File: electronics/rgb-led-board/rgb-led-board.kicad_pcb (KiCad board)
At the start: 2 copper layers, 24.1 x 17.8 mm, 12 parts, among them P1 PAD_SOLDER_2mm, P2 PAD_SOLDER_2mm, P3 CONN_01X08, P4 PAD_SOLDER_2mm, P5 PAD_SOLDER_2mm, P6 PAD_SOLDER_2mm, P7 PAD_SOLDER_2mm, U1 AL1793AFE-13

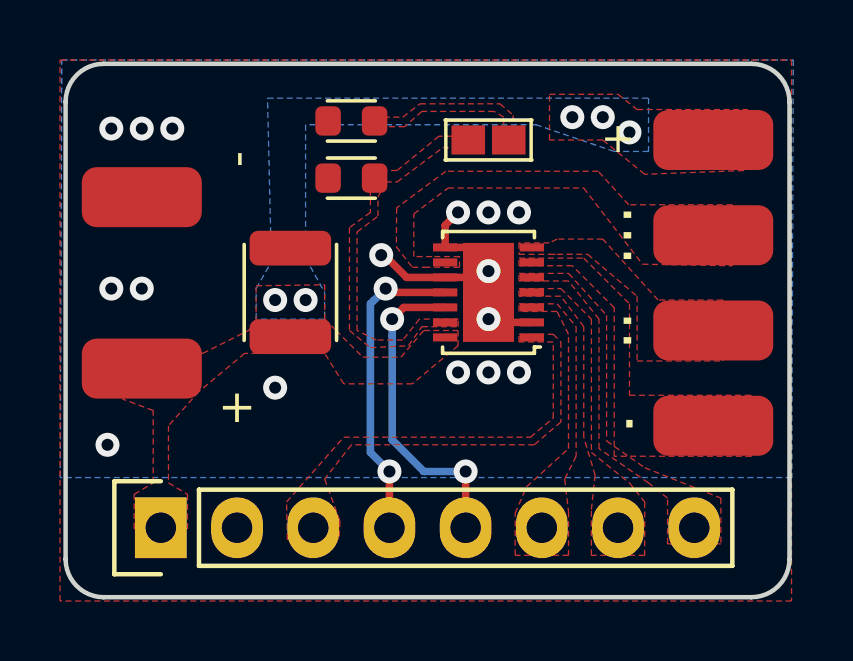
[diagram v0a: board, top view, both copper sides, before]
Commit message: Final changes to led driver board before gerbers
Minor annotation and titleblock contents
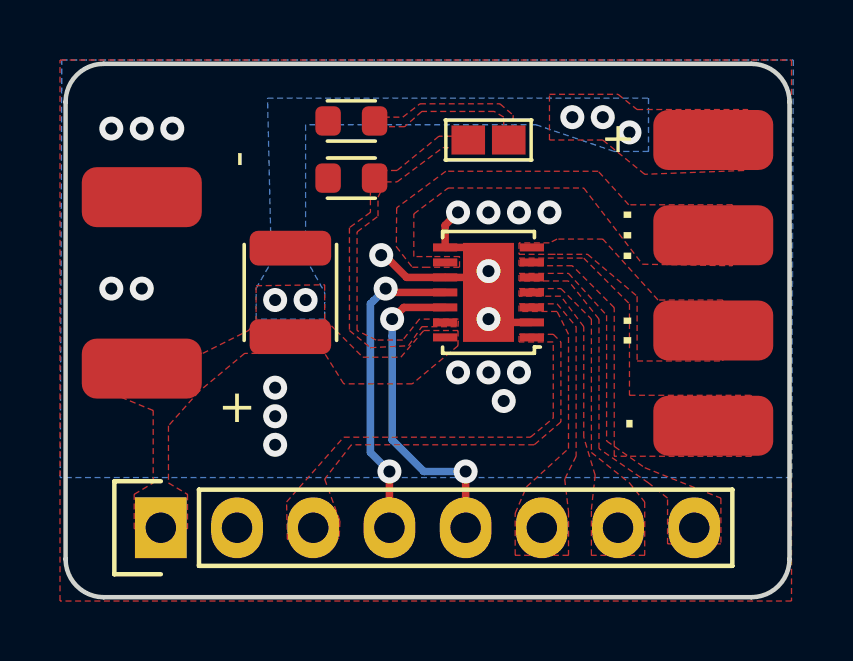
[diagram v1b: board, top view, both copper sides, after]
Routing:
- net GND: vias 16 -> 19
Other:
- board text added: "3x0.5A LED COMM ANODE SRAPSON 2018"
- board text added: "7-30V INPUT"
- board text added: "PCB Stackup 2 Layer 1.6mm FR4 ENIG Finish 25*18mm >0.35mm via drill >0.25mm clearance"
- board text removed: "2018 S.Rapson"
- board text removed: "max 30V"
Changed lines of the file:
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@@
   (general
     (thickness 1.6)
-    (drawings 24)
-    (tracks 52)
+    (drawings 27)
+    (tracks 55)
     (zones 0)
     (modules 12)
@@
   )
   (page A4)
+  (title_block
+    (title "3 channel common anode LED driver")
+    (date 2018-11-10)
+    (rev 1.0)
+    (company "Electric UI")
+    (comment 1 "Scott Rapson")
+  )
   (layers
     (0 F.Cu signal)
@@
     (visible_elements FFFDFF7F)
     (pcbplotparams
-      (layerselection 0x010fc_ffffffff)
-      (usegerberextensions false)
+      (layerselection 0x313fc_ffffffff)
+      (usegerberextensions true)
       (usegerberattributes false)
       (usegerberadvancedattributes false)
@@
       (outputformat 1)
       (mirror false)
-      (drillshape 1)
+      (drillshape 0)
       (scaleselection 1)
-      (outputdirectory ""))
+      (outputdirectory "Outputs/manf_exports/"))
   )
   (net 0 "")
@@
       (net 12 "Net-(R2-Pad1)"))
   )
-  (gr_text "2018\nS.Rapson" (at 144.145 58.547 90) (layer B.SilkS)
+  (gr_text "PCB Stackup\n\n2 Layer\n1.6mm FR4\nENIG Finish\n25*18mm\n>0.35mm via drill\n>0.25mm clearance" (at 157.0355 65.278) (layer Cmts.User)
+    (effects (font (size 1.5 1.5) (thickness 0.3)) (justify left))
+  )
+  (dimension 17.780113 (width 0.3) (layer Dwgs.User)
+    (gr_text "17.780 mm" (at 116.580656 66.69645 270.2046269) (layer Dwgs.User)
+      (effects (font (size 1.5 1.5) (thickness 0.3)))
+    )
+    (feature1 (pts (xy 122.6185 75.565) (xy 118.125976 75.581045)))
+    (feature2 (pts (xy 122.555 57.785) (xy 118.062476 57.801045)))
+    (crossbar (pts (xy 118.648893 57.79895) (xy 118.712393 75.57895)))
+    (arrow1a (pts (xy 118.712393 75.57895) (xy 118.121953 74.454548)))
+    (arrow1b (pts (xy 118.712393 75.57895) (xy 119.294787 74.450359)))
+    (arrow2a (pts (xy 118.648893 57.79895) (xy 118.066499 58.927541)))
+    (arrow2b (pts (xy 118.648893 57.79895) (xy 119.239333 58.923352)))
+  )
+  (dimension 24.1935 (width 0.3) (layer Dwgs.User)
+    (gr_text "24.194 mm" (at 134.65175 51.5575) (layer Dwgs.User)
+      (effects (font (size 1.5 1.5) (thickness 0.3)))
+    )
+    (feature1 (pts (xy 146.7485 57.7215) (xy 146.7485 53.071079)))
+    (feature2 (pts (xy 122.555 57.7215) (xy 122.555 53.071079)))
+    (crossbar (pts (xy 122.555 53.6575) (xy 146.7485 53.6575)))
+    (arrow1a (pts (xy 146.7485 53.6575) (xy 145.621996 54.243921)))
+    (arrow1b (pts (xy 146.7485 53.6575) (xy 145.621996 53.071079)))
+    (arrow2a (pts (xy 122.555 53.6575) (xy 123.681504 54.243921)))
+    (arrow2b (pts (xy 122.555 53.6575) (xy 123.681504 53.071079)))
+  )
+  (gr_text "3x0.5A LED\nCOMM ANODE\nSRAPSON 2018" (at 143.7005 58.3565 90) (layer B.SilkS)
     (effects (font (size 1 1) (thickness 0.18)) (justify left mirror))
   )
-  (gr_text "max\n30V" (at 127 63.5 90) (layer B.SilkS)
+  (gr_text "7-30V\nINPUT" (at 127 62.6745 90) (layer B.SilkS)
     (effects (font (size 1.2 1.2) (thickness 0.2)) (justify mirror))
   )
@@
   (segment (start 135.207 64.905) (end 136.152 64.905) (width 0.25) (layer F.Cu) (net 1))
   (via (at 137.668 68.072) (size 0.8) (drill 0.4) (layers F.Cu B.Cu) (net 1))
-  (via (at 123.952 70.485) (size 0.8) (drill 0.4) (layers F.Cu B.Cu) (net 1))
   (via (at 125.095 59.944) (size 0.8) (drill 0.4) (layers F.Cu B.Cu) (net 1))
   (via (at 124.079 59.944) (size 0.8) (drill 0.4) (layers F.Cu B.Cu) (net 1))
@@
   (via (at 133.075742 64.16189) (size 0.8) (drill 0.4) (layers F.Cu B.Cu) (net 1))
   (segment (start 133.24989 64.16189) (end 133.075742 64.16189) (width 0.25) (layer F.Cu) (net 1))
-  (via (at 139.446 59.563) (size 0.8) (drill 0.4) (layers F.Cu B.Cu) (net 2))
-  (via (at 140.462 59.563) (size 0.8) (drill 0.4) (layers F.Cu B.Cu) (net 2))
-  (via (at 141.351 60.071) (size 0.8) (drill 0.4) (layers F.Cu B.Cu) (net 2))
   (segment (start 133.179886 64.16189) (end 133.075742 64.16189) (width 0.25) (layer F.Cu) (net 1))
   (segment (start 133.922996 64.905) (end 133.179886 64.16189) (width 0.25) (layer F.Cu) (net 1))
@@
   (segment (start 135.207 63.905) (end 135.207 63.167) (width 0.25) (layer F.Cu) (net 1))
   (segment (start 135.207 63.167) (end 135.636 62.738) (width 0.25) (layer F.Cu) (net 1))
+  (via (at 129.54 69.5325) (size 0.8) (drill 0.4) (layers F.Cu B.Cu) (net 1))
+  (via (at 129.54 70.485) (size 0.8) (drill 0.4) (layers F.Cu B.Cu) (net 1))
+  (via (at 137.16 69.0245) (size 0.8) (drill 0.4) (layers F.Cu B.Cu) (net 1))
+  (via (at 138.684 62.738) (size 0.8) (drill 0.4) (layers F.Cu B.Cu) (net 1))
+  (via (at 139.446 59.563) (size 0.8) (drill 0.4) (layers F.Cu B.Cu) (net 2))
+  (via (at 140.462 59.563) (size 0.8) (drill 0.4) (layers F.Cu B.Cu) (net 2))
+  (via (at 141.351 60.071) (size 0.8) (drill 0.4) (layers F.Cu B.Cu) (net 2))
   (via (at 130.556 65.659) (size 0.8) (drill 0.4) (layers F.Cu B.Cu) (net 2))
   (via (at 129.54 65.659) (size 0.8) (drill 0.4) (layers F.Cu B.Cu) (net 2))
@@
     (polygon
       (pts
-        (xy 124.841 73.279) (xy 124.841 72.136) (xy 125.476 71.755) (xy 125.476 69.342) (xy 124.46 68.961)
-        (xy 124.46 67.437) (xy 127.127 67.437) (xy 128.651 66.675) (xy 128.905 66.38925) (xy 128.905 65.18275)
+        (xy 124.841 73.279) (xy 124.841 72.136) (xy 125.476 71.755) (xy 125.476 69.342) (xy 123.6345 68.58)
+        (xy 123.698 67.3735) (xy 127.127 67.437) (xy 128.651 66.675) (xy 128.905 66.38925) (xy 128.905 65.18275)
         (xy 131.191 65.151) (xy 131.191 66.294) (xy 131.572 66.675) (xy 132.461 67.564) (xy 133.731 67.564)
         (xy 134.493 66.675) (xy 135.636 66.675) (xy 135.636 67.183) (xy 134.112 68.453) (xy 131.826 68.453)
@@
     (polygon
       (pts
-        (xy 125.222 75.692) (xy 125.222 73.152) (xy 146.812 73.152) (xy 146.812 75.692)
+        (xy 124.46 75.692) (xy 124.46 73.152) (xy 146.812 73.152) (xy 146.812 75.692)
       )
     )
@@
     (min_thickness 0.25)
     (keepout (tracks allowed) (vias allowed) (copperpour not_allowed))
-    (fill (arc_segments 32) (thermal_gap 0.25) (thermal_bridge_width 0.3) (smoothing fillet) (radius 2))
+    (fill (arc_segments 32) (thermal_gap 0.25) (thermal_bridge_width 0.3))
     (polygon
       (pts
@@
     (min_thickness 0.3)
     (keepout (tracks allowed) (vias allowed) (copperpour not_allowed))
-    (fill (arc_segments 32) (thermal_gap 0.508) (thermal_bridge_width 0.508) (smoothing fillet) (radius 1.5))
-    (polygon
-      (pts
-        (xy 130.429 60.071) (xy 131.826 60.071) (xy 131.826 61.214) (xy 130.429 61.214)
+    (fill (arc_segments 32) (thermal_gap 0.508) (thermal_bridge_width 0.508))
+    (polygon
+      (pts
+        (xy 130.3655 60.071) (xy 131.7625 60.071) (xy 131.7625 61.214) (xy 130.3655 61.214)
       )
     )
@@
     (min_thickness 0.3)
     (keepout (tracks allowed) (vias allowed) (copperpour not_allowed))
-    (fill (arc_segments 32) (thermal_gap 0.508) (thermal_bridge_width 0.508) (smoothing fillet) (radius 2))
+    (fill (arc_segments 32) (thermal_gap 0.508) (thermal_bridge_width 0.508))
     (polygon
       (pts
@@
       )
     )
+  )
+  (zone (net 0) (net_name "") (layer F.Cu) (hatch edge 0.508)
+    (connect_pads yes (clearance 0.4))
+    (min_thickness 0.3)
+    (keepout (tracks allowed) (vias allowed) (copperpour not_allowed))
+    (fill (arc_segments 32) (thermal_gap 0.508) (thermal_bridge_width 0.508))
+    (polygon
+      (pts
+        (xy 130.3655 58.1025) (xy 131.7625 58.1025) (xy 131.7625 59.2455) (xy 130.3655 59.2455)
+      )
+    )
+  )
+  (zone (net 0) (net_name "") (layer F.Cu) (hatch edge 0.508)
+    (connect_pads yes (clearance 0.4))
+    (min_thickness 0.3)
+    (keepout (tracks allowed) (vias allowed) (copperpour not_allowed))
+    (fill (arc_segments 32) (thermal_gap 0.508) (thermal_bridge_width 0.508))
+    (polygon
+      (pts
+        (xy 130.3655 62.103) (xy 131.7625 62.103) (xy 131.7625 63.246) (xy 130.3655 63.246)
+      )
+    )
+  )
+  (zone (net 0) (net_name "") (layer F.Cu) (hatch edge 0.508)
+    (connect_pads yes (clearance 0.4))
+    (min_thickness 0.3)
+    (keepout (tracks allowed) (vias allowed) (copperpour not_allowed))
+    (fill (arc_segments 32) (thermal_gap 0.508) (thermal_bridge_width 0.508))
+    (polygon
+      (pts
+        (xy 128.2065 64.4525) (xy 128.778 64.4525) (xy 128.80975 66.6115) (xy 128.23825 66.6115)
+      )
+    )

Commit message: Reduced mask expansion to 0 for led-board
Allows fab to inflate as required.
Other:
- rule pad_to_mask_clearance: 0.2 -> 0
- board text added: "PCB Stackup 2 Layer 1.6mm FR4 ENIG Finish 25*18mm >0.35mm via drill >0.25mm clearance Inflate soldermask as required"
- board text removed: "PCB Stackup 2 Layer 1.6mm FR4 ENIG Finish 25*18mm >0.35mm via drill >0.25mm clearance"
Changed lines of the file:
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@@
     (pad_size 1.524 1.524)
     (pad_drill 0.762)
-    (pad_to_mask_clearance 0.2)
+    (pad_to_mask_clearance 0)
     (solder_mask_min_width 0.25)
     (aux_axis_origin 0 0)
@@
       (net 12 "Net-(R2-Pad1)"))
   )
-  (gr_text "PCB Stackup\n\n2 Layer\n1.6mm FR4\nENIG Finish\n25*18mm\n>0.35mm via drill\n>0.25mm clearance" (at 157.0355 65.278) (layer Cmts.User)
+  (gr_text "PCB Stackup\n\n2 Layer\n1.6mm FR4\nENIG Finish\n25*18mm\n>0.35mm via drill\n>0.25mm clearance\n\nInflate soldermask as required" (at 157.0355 65.278) (layer Cmts.User)
     (effects (font (size 1.5 1.5) (thickness 0.3)) (justify left))
   )
